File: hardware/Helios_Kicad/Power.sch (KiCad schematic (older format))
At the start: 10 parts, among them U2 AP2114, U3 AN431B, U4 ISA_DC-DC_converter

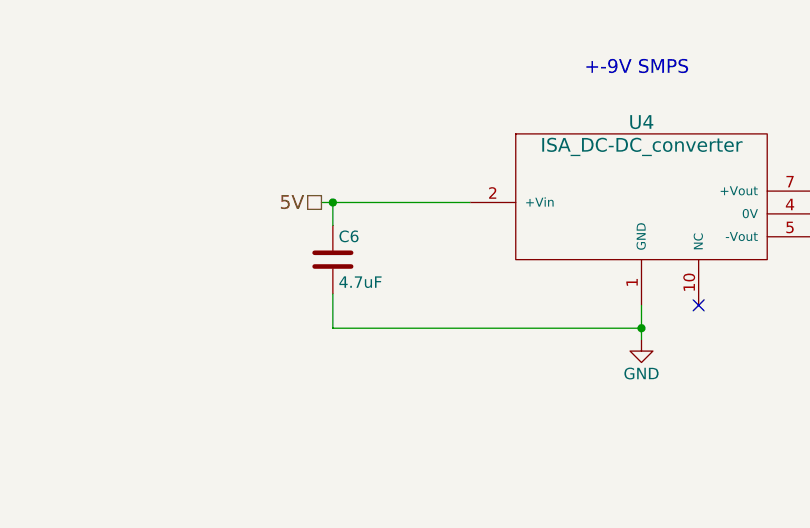
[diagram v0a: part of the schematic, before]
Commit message: driver finished but untested
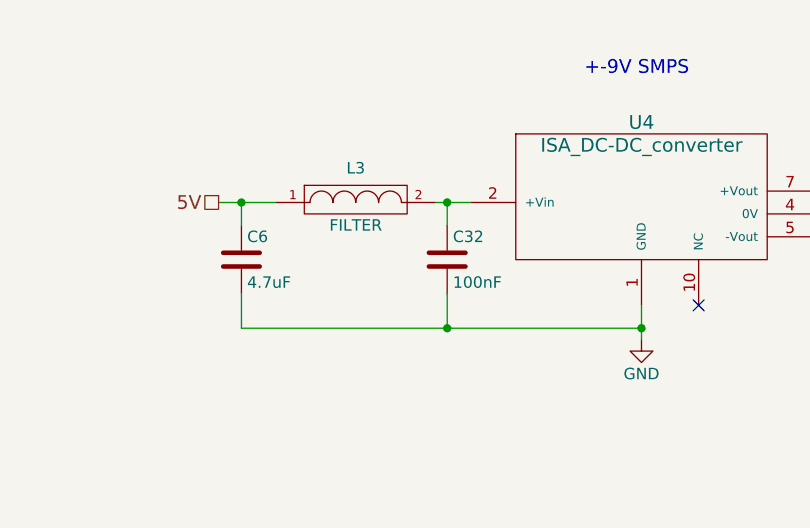
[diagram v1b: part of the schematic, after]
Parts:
- added C32: 100nF, symbol C
- added L3: FILTER, symbol FILTER
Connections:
- net 5V: now also L3.1; no longer U4.2 (+Vin)
- net GND: now also C32.2
- new net: C32.1, L3.2, U4.2 (+Vin)
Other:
- moved on the sheet: C6
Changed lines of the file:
@@
 $EndComp
 $Comp
-L GND #PWR07
+L GND #PWR7
 U 1 1 56EC0DF6
 P 3100 6150
-F 0 "#PWR07" H 3100 5900 50  0001 C CNN
+F 0 "#PWR7" H 3100 5900 50  0001 C CNN
 F 1 "GND" H 3100 6000 50  0000 C CNN
 F 2 "" H 3100 6150 50  0000 C CNN
@@
 Text HLabel 2300 5200 0    60   UnSpc ~ 0
 3.3V
-Text HLabel 6100 2450 0    60   UnSpc ~ 0
+Text HLabel 5650 2450 0    60   UnSpc ~ 0
 5V
 $Comp
-L GND #PWR08
+L GND #PWR9
 U 1 1 56ED02CC
 P 7500 3050
-F 0 "#PWR08" H 7500 2800 50  0001 C CNN
+F 0 "#PWR9" H 7500 2800 50  0001 C CNN
 F 1 "GND" H 7500 2900 50  0000 C CNN
 F 2 "" H 7500 3050 50  0000 C CNN
@@
 $EndComp
 $Comp
-L GND #PWR09
+L GND #PWR10
 U 1 1 56ED03CC
 P 8350 2500
-F 0 "#PWR09" H 8350 2250 50  0001 C CNN
+F 0 "#PWR10" H 8350 2250 50  0001 C CNN
 F 1 "GND" H 8350 2350 50  0000 C CNN
 F 2 "" H 8350 2500 50  0000 C CNN
@@
 -9V
 $Comp
-L GND #PWR010
+L GND #PWR12
 U 1 1 5703D8E0
 P 8550 2950
-F 0 "#PWR010" H 8550 2700 50  0001 C CNN
+F 0 "#PWR12" H 8550 2700 50  0001 C CNN
 F 1 "GND" H 8550 2800 50  0000 C CNN
 F 2 "" H 8550 2950 50  0000 C CNN
@@
 $EndComp
 $Comp
-L GND #PWR011
+L GND #PWR11
 U 1 1 5703D96C
 P 8550 2050
-F 0 "#PWR011" H 8550 1800 50  0001 C CNN
+F 0 "#PWR11" H 8550 1800 50  0001 C CNN
 F 1 "GND" H 8550 1900 50  0000 C CNN
 F 2 "" H 8550 2050 50  0000 C CNN
@@
 L C C6
 U 1 1 57365067
-P 6150 2700
-F 0 "C6" H 6175 2800 50  0000 L CNN
-F 1 "4.7uF" H 6175 2600 50  0000 L CNN
-F 2 "Capacitors_SMD:C_0805" H 6188 2550 50  0001 C CNN
-F 3 "" H 6150 2700 50  0000 C CNN
-	1    6150 2700
+P 5750 2700
+F 0 "C6" H 5775 2800 50  0000 L CNN
+F 1 "4.7uF" H 5775 2600 50  0000 L CNN
+F 2 "Capacitors_SMD:C_0805" H 5788 2550 50  0001 C CNN
+F 3 "" H 5750 2700 50  0000 C CNN
+	1    5750 2700
 	1    0    0    -1
 $EndComp
@@
 $EndComp
 $Comp
-L GND #PWR012
+L GND #PWR8
 U 1 1 573CF740
 P 3350 3050
-F 0 "#PWR012" H 3350 2800 50  0001 C CNN
+F 0 "#PWR8" H 3350 2800 50  0001 C CNN
 F 1 "GND" H 3350 2900 50  0000 C CNN
 F 2 "" H 3350 3050 50  0000 C CNN
@@
 Text Notes 1750 6500 0    60   ~ 0
 Shunt reference is UNSTABLE when bypassed with 10^3 to 10^6 pF so 100nF can't be used alone
-Wire Wire Line
-	1600 2250 2200 2250
-Wire Wire Line
-	1950 2200 1950 2400
-Connection ~ 1950 2250
-Wire Wire Line
-	1950 2700 1950 2950
-Wire Wire Line
-	1950 2950 3400 2950
-Wire Wire Line
-	3400 2950 3400 2750
-Wire Wire Line
-	3400 2450 3400 2250
-Wire Wire Line
-	3100 2250 3750 2250
-Connection ~ 3400 2250
-Wire Wire Line
-	2700 5200 4650 5200
-Wire Wire Line
-	3100 5200 3100 5450
-Wire Wire Line
-	3100 5350 2650 5350
-Wire Wire Line
-	2650 5350 2650 5800
-Wire Wire Line
-	2650 5800 2800 5800
-Connection ~ 3100 5350
-Connection ~ 3100 5200
-Wire Wire Line
-	2400 5200 2300 5200
-Wire Wire Line
-	6150 3000 7500 3000
-Wire Wire Line
-	7500 2900 7500 3050
-Connection ~ 7500 3000
-Wire Wire Line
-	8250 2400 8650 2400
-Wire Wire Line
-	8250 2600 8650 2600
-Wire Wire Line
-	8250 2500 8350 2500
-Wire Wire Line
-	8550 2350 8550 2400
-Connection ~ 8550 2400
-Wire Wire Line
-	8550 2650 8550 2600
-Connection ~ 8550 2600
-Wire Wire Line
-	6100 2450 6750 2450
-Wire Wire Line
-	6150 3000 6150 2850
-Wire Wire Line
-	6150 2550 6150 2450
-Connection ~ 6150 2450
-Wire Wire Line
-	3350 2950 3350 3050
-Connection ~ 3350 2950
-Wire Wire Line
-	2650 2750 2650 2950
-Connection ~ 2650 2950
-$Comp
-L PWR_FLAG #FLG013
+$Comp
+L PWR_FLAG #FLG1
 U 1 1 575B50A4
 P 1950 2200
-F 0 "#FLG013" H 1950 2295 50  0001 C CNN
+F 0 "#FLG1" H 1950 2295 50  0001 C CNN
 F 1 "PWR_FLAG" H 1950 2380 50  0000 C CNN
 F 2 "" H 1950 2200 50  0000 C CNN
@@
 	0    -1   -1   0
 $EndComp
+$Comp
+L FILTER L3
+U 1 1 578632B6
+P 6250 2450
+F 0 "L3" H 6250 2600 50  0000 C CNN
+F 1 "FILTER" H 6250 2350 50  0000 C CNN
+F 2 "" H 6250 2450 50  0000 C CNN
+F 3 "" H 6250 2450 50  0000 C CNN
+	1    6250 2450
+	1    0    0    -1
+$EndComp
+Wire Wire Line
+	1600 2250 2200 2250
+Wire Wire Line
+	1950 2200 1950 2400
+Connection ~ 1950 2250
+Wire Wire Line
+	1950 2700 1950 2950
+Wire Wire Line
+	1950 2950 3400 2950
+Wire Wire Line
+	3400 2950 3400 2750
+Wire Wire Line
+	3400 2450 3400 2250
+Wire Wire Line
+	3100 2250 3750 2250
+Connection ~ 3400 2250
+Wire Wire Line
+	2700 5200 4650 5200
+Wire Wire Line
+	3100 5200 3100 5450
+Wire Wire Line
+	3100 5350 2650 5350
+Wire Wire Line
+	2650 5350 2650 5800
+Wire Wire Line
+	2650 5800 2800 5800
+Connection ~ 3100 5350
+Connection ~ 3100 5200
+Wire Wire Line
+	2400 5200 2300 5200
+Wire Wire Line
+	5750 3000 7500 3000
+Wire Wire Line
+	7500 2900 7500 3050
+Connection ~ 7500 3000
+Wire Wire Line
+	8250 2400 8650 2400
+Wire Wire Line
+	8250 2600 8650 2600
+Wire Wire Line
+	8250 2500 8350 2500
+Wire Wire Line
+	8550 2350 8550 2400
+Connection ~ 8550 2400
+Wire Wire Line
+	8550 2650 8550 2600
+Connection ~ 8550 2600
+Wire Wire Line
+	3350 2950 3350 3050
+Connection ~ 3350 2950
+Wire Wire Line
+	2650 2750 2650 2950
+Connection ~ 2650 2950
 Wire Wire Line
 	2400 5000 2400 5200
 Wire Wire Line
 	2700 5000 2700 5200
+Wire Wire Line
+	6750 2450 6600 2450
+Wire Wire Line
+	5750 3000 5750 2850
+Wire Wire Line
+	5750 2550 5750 2450
+Wire Wire Line
+	5650 2450 5900 2450
+Connection ~ 5750 2450
+$Comp
+L C C32
+U 1 1 57863537
+P 6650 2700
+F 0 "C32" H 6675 2800 50  0000 L CNN
+F 1 "100nF" H 6675 2600 50  0000 L CNN
+F 2 "" H 6688 2550 50  0001 C CNN
+F 3 "" H 6650 2700 50  0000 C CNN
+	1    6650 2700
+	1    0    0    -1
+$EndComp
+Wire Wire Line
+	6650 2550 6650 2450
+Connection ~ 6650 2450
+Wire Wire Line
+	6650 2850 6650 3000
+Connection ~ 6650 3000
 $EndSCHEMATC

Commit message: redone pcb, driver and firmware working-ish
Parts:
- C4, C5, C6: footprint Capacitors_SMD:C_0805 -> Capacitors_SMD:C_0603
- C7: renamed from C32; footprint (none) -> Capacitors_SMD:C_0402
- C8: renamed from C7; footprint Capacitors_SMD:C_0805 -> Capacitors_SMD:C_0603
- C9: renamed from C8; footprint Capacitors_SMD:C_0805 -> Capacitors_SMD:C_0603
- L2: renamed from L3; footprint (none) -> Resistors_SMD:R_0603
- renumbered R16 to R12, R17 to R13
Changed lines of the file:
@@
 LIBS:valves
 LIBS:Personal library
+LIBS:Helios-cache
 EELAYER 25 0
 EELAYER END
@@
 3.3V
 $Comp
-L R R17
+L R R13
 U 1 1 56EC07CE
 P 2550 5200
-F 0 "R17" V 2630 5200 50  0000 C CNN
+F 0 "R13" V 2630 5200 50  0000 C CNN
 F 1 "150" V 2550 5200 50  0000 C CNN
 F 2 "Resistors_SMD:R_0603" V 2480 5200 50  0001 C CNN
@@
 $EndComp
 $Comp
-L GND #PWR7
+L GND #PWR07
 U 1 1 56EC0DF6
 P 3100 6150
-F 0 "#PWR7" H 3100 5900 50  0001 C CNN
+F 0 "#PWR07" H 3100 5900 50  0001 C CNN
 F 1 "GND" H 3100 6000 50  0000 C CNN
 F 2 "" H 3100 6150 50  0000 C CNN
@@
 5V
 $Comp
-L GND #PWR9
+L GND #PWR08
 U 1 1 56ED02CC
 P 7500 3050
-F 0 "#PWR9" H 7500 2800 50  0001 C CNN
+F 0 "#PWR08" H 7500 2800 50  0001 C CNN
 F 1 "GND" H 7500 2900 50  0000 C CNN
 F 2 "" H 7500 3050 50  0000 C CNN
@@
 $EndComp
 $Comp
-L GND #PWR10
+L GND #PWR09
 U 1 1 56ED03CC
 P 8350 2500
-F 0 "#PWR10" H 8350 2250 50  0001 C CNN
+F 0 "#PWR09" H 8350 2250 50  0001 C CNN
 F 1 "GND" H 8350 2350 50  0000 C CNN
 F 2 "" H 8350 2500 50  0000 C CNN
@@
 -9V
 $Comp
-L GND #PWR12
+L GND #PWR010
 U 1 1 5703D8E0
 P 8550 2950
-F 0 "#PWR12" H 8550 2700 50  0001 C CNN
+F 0 "#PWR010" H 8550 2700 50  0001 C CNN
 F 1 "GND" H 8550 2800 50  0000 C CNN
 F 2 "" H 8550 2950 50  0000 C CNN
@@
 $EndComp
 $Comp
-L GND #PWR11
+L GND #PWR011
 U 1 1 5703D96C
 P 8550 2050
-F 0 "#PWR11" H 8550 1800 50  0001 C CNN
+F 0 "#PWR011" H 8550 1800 50  0001 C CNN
 F 1 "GND" H 8550 1900 50  0000 C CNN
 F 2 "" H 8550 2050 50  0000 C CNN
@@
 F 0 "C5" H 3425 2700 50  0000 L CNN
 F 1 "4.7uF" H 3425 2500 50  0000 L CNN
-F 2 "Capacitors_SMD:C_0805" H 3438 2450 50  0001 C CNN
+F 2 "Capacitors_SMD:C_0603" H 3438 2450 50  0001 C CNN
 F 3 "" H 3400 2600 50  0000 C CNN
 	1    3400 2600
@@
 NoConn ~ 7750 2900
 $Comp
-L C C7
+L C C8
 U 1 1 57390D8D
 P 8550 2200
-F 0 "C7" H 8575 2300 50  0000 L CNN
+F 0 "C8" H 8575 2300 50  0000 L CNN
 F 1 "4.7uF" H 8575 2100 50  0000 L CNN
-F 2 "Capacitors_SMD:C_0805" H 8588 2050 50  0001 C CNN
+F 2 "Capacitors_SMD:C_0603" H 8588 2050 50  0001 C CNN
 F 3 "" H 8550 2200 50  0000 C CNN
 	1    8550 2200
@@
 $EndComp
 $Comp
-L C C8
+L C C9
 U 1 1 57390DDD
 P 8550 2800
-F 0 "C8" H 8575 2900 50  0000 L CNN
+F 0 "C9" H 8575 2900 50  0000 L CNN
 F 1 "4.7uF" H 8575 2700 50  0000 L CNN
-F 2 "Capacitors_SMD:C_0805" H 8588 2650 50  0001 C CNN
+F 2 "Capacitors_SMD:C_0603" H 8588 2650 50  0001 C CNN
 F 3 "" H 8550 2800 50  0000 C CNN
 	1    8550 2800
@@
 F 0 "C6" H 5775 2800 50  0000 L CNN
 F 1 "4.7uF" H 5775 2600 50  0000 L CNN
-F 2 "Capacitors_SMD:C_0805" H 5788 2550 50  0001 C CNN
+F 2 "Capacitors_SMD:C_0603" H 5788 2550 50  0001 C CNN
 F 3 "" H 5750 2700 50  0000 C CNN
 	1    5750 2700
@@
 F 0 "C4" H 1975 2650 50  0000 L CNN
 F 1 "4.7uF" H 1975 2450 50  0000 L CNN
-F 2 "Capacitors_SMD:C_0805" H 1988 2400 50  0001 C CNN
+F 2 "Capacitors_SMD:C_0603" H 1988 2400 50  0001 C CNN
 F 3 "" H 1950 2550 50  0000 C CNN
 	1    1950 2550
@@
 $EndComp
 $Comp
-L GND #PWR8
+L GND #PWR012
 U 1 1 573CF740
 P 3350 3050
-F 0 "#PWR8" H 3350 2800 50  0001 C CNN
+F 0 "#PWR012" H 3350 2800 50  0001 C CNN
 F 1 "GND" H 3350 2900 50  0000 C CNN
 F 2 "" H 3350 3050 50  0000 C CNN
@@
 Shunt reference is UNSTABLE when bypassed with 10^3 to 10^6 pF so 100nF can't be used alone
 $Comp
-L PWR_FLAG #FLG1
+L PWR_FLAG #FLG013
 U 1 1 575B50A4
 P 1950 2200
-F 0 "#FLG1" H 1950 2295 50  0001 C CNN
+F 0 "#FLG013" H 1950 2295 50  0001 C CNN
 F 1 "PWR_FLAG" H 1950 2380 50  0000 C CNN
 F 2 "" H 1950 2200 50  0000 C CNN
@@
 $EndComp
 $Comp
-L R R16
+L R R12
 U 1 1 575C427B
 P 2550 5000
-F 0 "R16" V 2630 5000 50  0000 C CNN
+F 0 "R12" V 2630 5000 50  0000 C CNN
 F 1 "150" V 2550 5000 50  0000 C CNN
 F 2 "Resistors_SMD:R_0603" V 2480 5000 50  0001 C CNN
@@
 $EndComp
 $Comp
-L FILTER L3
+L FILTER L2
 U 1 1 578632B6
 P 6250 2450
-F 0 "L3" H 6250 2600 50  0000 C CNN
+F 0 "L2" H 6250 2600 50  0000 C CNN
 F 1 "FILTER" H 6250 2350 50  0000 C CNN
-F 2 "" H 6250 2450 50  0000 C CNN
+F 2 "Resistors_SMD:R_0603" H 6250 2450 50  0001 C CNN
 F 3 "" H 6250 2450 50  0000 C CNN
 	1    6250 2450
@@
 Connection ~ 5750 2450
 $Comp
-L C C32
+L C C7
 U 1 1 57863537
 P 6650 2700
-F 0 "C32" H 6675 2800 50  0000 L CNN
+F 0 "C7" H 6675 2800 50  0000 L CNN
 F 1 "100nF" H 6675 2600 50  0000 L CNN
-F 2 "" H 6688 2550 50  0001 C CNN
+F 2 "Capacitors_SMD:C_0402" H 6688 2550 50  0001 C CNN
 F 3 "" H 6650 2700 50  0000 C CNN
 	1    6650 2700
@@
 	6650 2850 6650 3000
 Connection ~ 6650 3000
+$Comp
+L PWR_FLAG #FLG014
+U 1 1 5792E8E7
+P 6750 2400
+F 0 "#FLG014" H 6750 2495 50  0001 C CNN
+F 1 "PWR_FLAG" H 6750 2580 50  0000 C CNN
+F 2 "" H 6750 2400 50  0000 C CNN
+F 3 "" H 6750 2400 50  0000 C CNN
+	1    6750 2400
+	1    0    0    -1
+$EndComp
+Wire Wire Line
+	6750 2400 6750 2450
 $EndSCHEMATC

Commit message: rev 1.1 pcb final
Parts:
- removed C5: 4.7uF, Capacitors_SMD:C_0603, symbol C
- C4, C6, C8, C9: footprint Capacitors_SMD:C_0603 -> Capacitors_SMD:c_elec_4x5.3
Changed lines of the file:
@@
 $EndComp
 $Comp
-L GND #PWR07
+L GND #PWR7
 U 1 1 56EC0DF6
 P 3100 6150
-F 0 "#PWR07" H 3100 5900 50  0001 C CNN
+F 0 "#PWR7" H 3100 5900 50  0001 C CNN
 F 1 "GND" H 3100 6000 50  0000 C CNN
 F 2 "" H 3100 6150 50  0000 C CNN
@@
 5V
 $Comp
-L GND #PWR08
+L GND #PWR9
 U 1 1 56ED02CC
 P 7500 3050
-F 0 "#PWR08" H 7500 2800 50  0001 C CNN
+F 0 "#PWR9" H 7500 2800 50  0001 C CNN
 F 1 "GND" H 7500 2900 50  0000 C CNN
 F 2 "" H 7500 3050 50  0000 C CNN
@@
 $EndComp
 $Comp
-L GND #PWR09
+L GND #PWR10
 U 1 1 56ED03CC
 P 8350 2500
-F 0 "#PWR09" H 8350 2250 50  0001 C CNN
+F 0 "#PWR10" H 8350 2250 50  0001 C CNN
 F 1 "GND" H 8350 2350 50  0000 C CNN
 F 2 "" H 8350 2500 50  0000 C CNN
@@
 -9V
 $Comp
-L GND #PWR010
+L GND #PWR12
 U 1 1 5703D8E0
 P 8550 2950
-F 0 "#PWR010" H 8550 2700 50  0001 C CNN
+F 0 "#PWR12" H 8550 2700 50  0001 C CNN
 F 1 "GND" H 8550 2800 50  0000 C CNN
 F 2 "" H 8550 2950 50  0000 C CNN
@@
 $EndComp
 $Comp
-L GND #PWR011
+L GND #PWR11
 U 1 1 5703D96C
 P 8550 2050
-F 0 "#PWR011" H 8550 1800 50  0001 C CNN
+F 0 "#PWR11" H 8550 1800 50  0001 C CNN
 F 1 "GND" H 8550 1900 50  0000 C CNN
 F 2 "" H 8550 2050 50  0000 C CNN
@@
 Text Notes 2700 4700 0    60   ~ 0
 2.5V Reference\n
-$Comp
-L C C5
-U 1 1 57364A03
-P 3400 2600
-F 0 "C5" H 3425 2700 50  0000 L CNN
-F 1 "4.7uF" H 3425 2500 50  0000 L CNN
-F 2 "Capacitors_SMD:C_0603" H 3438 2450 50  0001 C CNN
-F 3 "" H 3400 2600 50  0000 C CNN
-	1    3400 2600
-	1    0    0    -1
-$EndComp
 $Comp
 L ISA_DC-DC_converter U4
@@
 F 0 "C8" H 8575 2300 50  0000 L CNN
 F 1 "4.7uF" H 8575 2100 50  0000 L CNN
-F 2 "Capacitors_SMD:C_0603" H 8588 2050 50  0001 C CNN
+F 2 "Capacitors_SMD:c_elec_4x5.3" H 8588 2050 50  0001 C CNN
 F 3 "" H 8550 2200 50  0000 C CNN
 	1    8550 2200
@@
 F 0 "C9" H 8575 2900 50  0000 L CNN
 F 1 "4.7uF" H 8575 2700 50  0000 L CNN
-F 2 "Capacitors_SMD:C_0603" H 8588 2650 50  0001 C CNN
+F 2 "Capacitors_SMD:c_elec_4x5.3" H 8588 2650 50  0001 C CNN
 F 3 "" H 8550 2800 50  0000 C CNN
 	1    8550 2800
@@
 F 0 "C6" H 5775 2800 50  0000 L CNN
 F 1 "4.7uF" H 5775 2600 50  0000 L CNN
-F 2 "Capacitors_SMD:C_0603" H 5788 2550 50  0001 C CNN
+F 2 "Capacitors_SMD:c_elec_4x5.3" H 5788 2550 50  0001 C CNN
 F 3 "" H 5750 2700 50  0000 C CNN
 	1    5750 2700
@@
 F 0 "C4" H 1975 2650 50  0000 L CNN
 F 1 "4.7uF" H 1975 2450 50  0000 L CNN
-F 2 "Capacitors_SMD:C_0603" H 1988 2400 50  0001 C CNN
+F 2 "Capacitors_SMD:c_elec_4x5.3" H 1988 2400 50  0001 C CNN
 F 3 "" H 1950 2550 50  0000 C CNN
 	1    1950 2550
@@
 $EndComp
 $Comp
-L GND #PWR012
+L GND #PWR8
 U 1 1 573CF740
 P 3350 3050
-F 0 "#PWR012" H 3350 2800 50  0001 C CNN
+F 0 "#PWR8" H 3350 2800 50  0001 C CNN
 F 1 "GND" H 3350 2900 50  0000 C CNN
 F 2 "" H 3350 3050 50  0000 C CNN
@@
 Shunt reference is UNSTABLE when bypassed with 10^3 to 10^6 pF so 100nF can't be used alone
 $Comp
-L PWR_FLAG #FLG013
+L PWR_FLAG #FLG1
 U 1 1 575B50A4
 P 1950 2200
-F 0 "#FLG013" H 1950 2295 50  0001 C CNN
+F 0 "#FLG1" H 1950 2295 50  0001 C CNN
 F 1 "PWR_FLAG" H 1950 2380 50  0000 C CNN
 F 2 "" H 1950 2200 50  0000 C CNN
@@
 	1950 2700 1950 2950
 Wire Wire Line
-	1950 2950 3400 2950
-Wire Wire Line
-	3400 2950 3400 2750
-Wire Wire Line
-	3400 2450 3400 2250
-Wire Wire Line
 	3100 2250 3750 2250
-Connection ~ 3400 2250
 Wire Wire Line
 	2700 5200 4650 5200
@@
 Wire Wire Line
 	3350 2950 3350 3050
-Connection ~ 3350 2950
 Wire Wire Line
 	2650 2750 2650 2950
@@
 Connection ~ 6650 3000
 $Comp
-L PWR_FLAG #FLG014
+L PWR_FLAG #FLG2
 U 1 1 5792E8E7
 P 6750 2400
-F 0 "#FLG014" H 6750 2495 50  0001 C CNN
+F 0 "#FLG2" H 6750 2495 50  0001 C CNN
 F 1 "PWR_FLAG" H 6750 2580 50  0000 C CNN
 F 2 "" H 6750 2400 50  0000 C CNN
@@
 Wire Wire Line
 	6750 2400 6750 2450
+Wire Wire Line
+	1950 2950 3350 2950
 $EndSCHEMATC

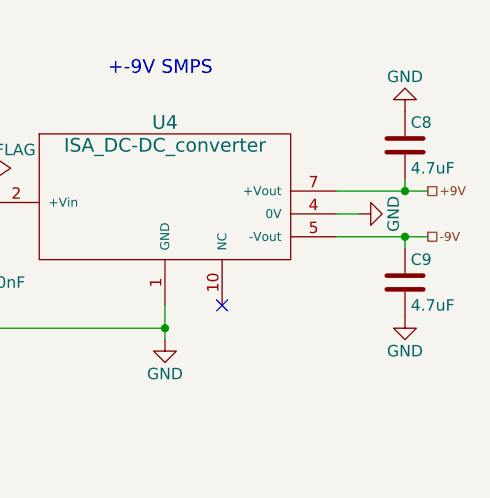
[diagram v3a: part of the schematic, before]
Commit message: capacitors wrong polarity
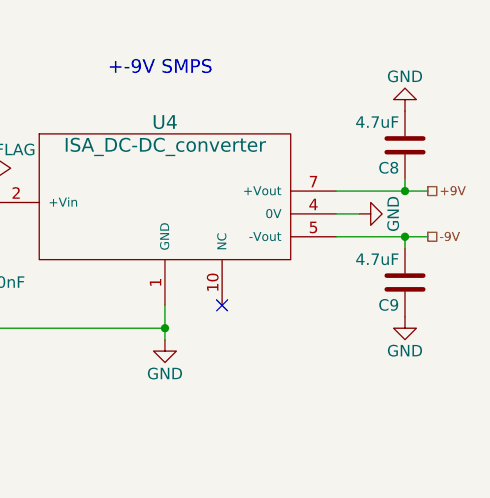
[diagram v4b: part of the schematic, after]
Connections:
- net +9V: now also C8.1; no longer C8.2
- net -9V: now also C9.2; no longer C9.1
- net GND: now also C8.2, C9.1; no longer C8.1, C9.2
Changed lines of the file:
@@
 $EndComp
 $Comp
-L GND #PWR7
+L GND #PWR07
 U 1 1 56EC0DF6
 P 3100 6150
-F 0 "#PWR7" H 3100 5900 50  0001 C CNN
+F 0 "#PWR07" H 3100 5900 50  0001 C CNN
 F 1 "GND" H 3100 6000 50  0000 C CNN
 F 2 "" H 3100 6150 50  0000 C CNN
@@
 5V
 $Comp
-L GND #PWR9
+L GND #PWR08
 U 1 1 56ED02CC
 P 7500 3050
-F 0 "#PWR9" H 7500 2800 50  0001 C CNN
+F 0 "#PWR08" H 7500 2800 50  0001 C CNN
 F 1 "GND" H 7500 2900 50  0000 C CNN
 F 2 "" H 7500 3050 50  0000 C CNN
@@
 $EndComp
 $Comp
-L GND #PWR10
+L GND #PWR09
 U 1 1 56ED03CC
 P 8350 2500
-F 0 "#PWR10" H 8350 2250 50  0001 C CNN
+F 0 "#PWR09" H 8350 2250 50  0001 C CNN
 F 1 "GND" H 8350 2350 50  0000 C CNN
 F 2 "" H 8350 2500 50  0000 C CNN
@@
 -9V
 $Comp
-L GND #PWR12
+L GND #PWR010
 U 1 1 5703D8E0
 P 8550 2950
-F 0 "#PWR12" H 8550 2700 50  0001 C CNN
+F 0 "#PWR010" H 8550 2700 50  0001 C CNN
 F 1 "GND" H 8550 2800 50  0000 C CNN
 F 2 "" H 8550 2950 50  0000 C CNN
@@
 $EndComp
 $Comp
-L GND #PWR11
+L GND #PWR011
 U 1 1 5703D96C
 P 8550 2050
-F 0 "#PWR11" H 8550 1800 50  0001 C CNN
+F 0 "#PWR011" H 8550 1800 50  0001 C CNN
 F 1 "GND" H 8550 1900 50  0000 C CNN
 F 2 "" H 8550 2050 50  0000 C CNN
@@
 F 3 "" H 8550 2200 50  0000 C CNN
 	1    8550 2200
-	1    0    0    -1
+	-1   0    0    1
 $EndComp
 $Comp
@@
 F 3 "" H 8550 2800 50  0000 C CNN
 	1    8550 2800
-	1    0    0    -1
+	-1   0    0    1
 $EndComp
 $Comp
@@
 $EndComp
 $Comp
-L GND #PWR8
+L GND #PWR012
 U 1 1 573CF740
 P 3350 3050
-F 0 "#PWR8" H 3350 2800 50  0001 C CNN
+F 0 "#PWR012" H 3350 2800 50  0001 C CNN
 F 1 "GND" H 3350 2900 50  0000 C CNN
 F 2 "" H 3350 3050 50  0000 C CNN
@@
 Shunt reference is UNSTABLE when bypassed with 10^3 to 10^6 pF so 100nF can't be used alone
 $Comp
-L PWR_FLAG #FLG1
+L PWR_FLAG #FLG013
 U 1 1 575B50A4
 P 1950 2200
-F 0 "#FLG1" H 1950 2295 50  0001 C CNN
+F 0 "#FLG013" H 1950 2295 50  0001 C CNN
 F 1 "PWR_FLAG" H 1950 2380 50  0000 C CNN
 F 2 "" H 1950 2200 50  0000 C CNN
@@
 Connection ~ 6650 3000
 $Comp
-L PWR_FLAG #FLG2
+L PWR_FLAG #FLG014
 U 1 1 5792E8E7
 P 6750 2400
-F 0 "#FLG2" H 6750 2495 50  0001 C CNN
+F 0 "#FLG014" H 6750 2495 50  0001 C CNN
 F 1 "PWR_FLAG" H 6750 2580 50  0000 C CNN
 F 2 "" H 6750 2400 50  0000 C CNN
